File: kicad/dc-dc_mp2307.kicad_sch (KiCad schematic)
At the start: 20 parts

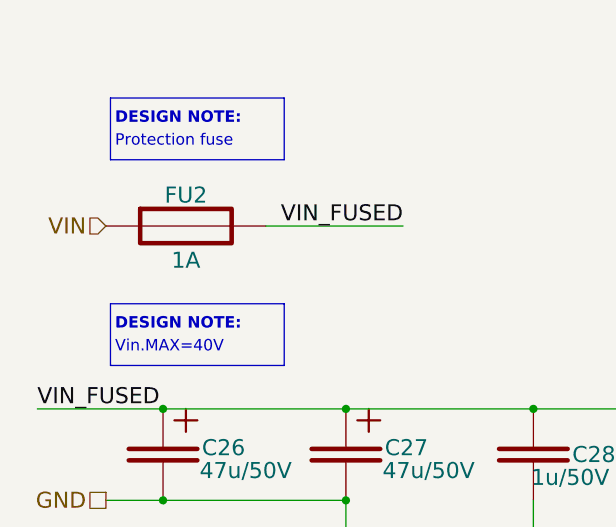
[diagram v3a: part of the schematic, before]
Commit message: Add Vin.MIN=5.5V to schematic DC-DC note
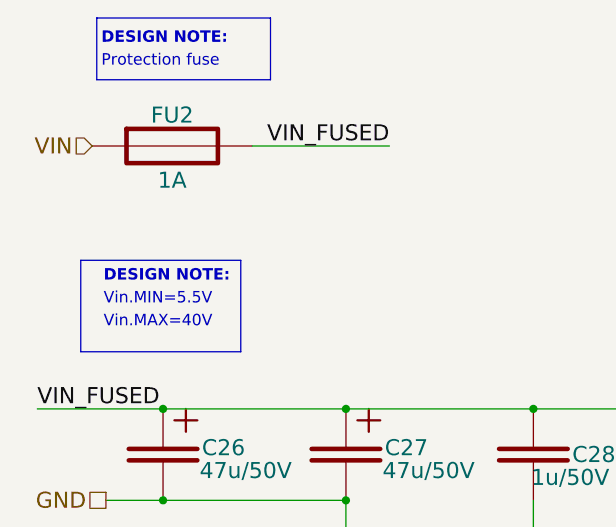
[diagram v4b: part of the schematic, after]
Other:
- note added: "Vin.MIN=5.5V"
- moved on the sheet: FU2
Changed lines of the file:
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@@
   (junction (at 78.232 69.85) (diameter 0) (color 0 0 0 0)
   )
-  (polyline (pts (xy 50.546 42.164) (xy 31.242 42.164))
+  (polyline (pts (xy 49.022 33.274) (xy 29.718 33.274))
     (stroke (width 0) (type default) (color 0 132 132 1))
   )
@@
     (stroke (width 0) (type default) (color 0 0 0 0))
   )
-  (polyline (pts (xy 31.242 58.166) (xy 31.242 65.024))
+  (polyline (pts (xy 27.94 53.34) (xy 27.94 63.5))
     (stroke (width 0) (type default) (color 0 132 132 1))
   )
@@
     (stroke (width 0) (type default) (color 0 0 0 0))
   )
-  (polyline (pts (xy 50.546 65.024) (xy 31.242 65.024))
+  (polyline (pts (xy 45.72 63.5) (xy 27.94 63.5))
     (stroke (width 0) (type default) (color 0 132 132 1))
   )
@@
     (stroke (width 0) (type default) (color 0 0 0 0))
   )
-  (polyline (pts (xy 50.546 35.306) (xy 50.546 42.164))
+  (polyline (pts (xy 49.022 26.416) (xy 49.022 33.274))
     (stroke (width 0) (type default) (color 0 132 132 1))
   )
@@
     (stroke (width 0) (type default) (color 0 0 0 0))
   )
-  (polyline (pts (xy 31.242 35.306) (xy 31.242 42.164))
+  (polyline (pts (xy 29.718 26.416) (xy 29.718 33.274))
     (stroke (width 0) (type default) (color 0 132 132 1))
   )
@@
     (stroke (width 0) (type default) (color 0 0 0 0))
   )
-  (polyline (pts (xy 50.546 58.166) (xy 50.546 65.024))
+  (polyline (pts (xy 45.72 53.34) (xy 45.72 63.5))
     (stroke (width 0) (type default) (color 0 132 132 1))
   )
@@
     (stroke (width 0) (type default) (color 0 0 0 0))
   )
-  (wire (pts (xy 48.514 49.53) (xy 63.754 49.53))
+  (wire (pts (xy 46.99 40.64) (xy 62.23 40.64))
     (stroke (width 0) (type default) (color 0 0 0 0))
   )
@@
     (stroke (width 0) (type default) (color 0 0 0 0))
   )
-  (polyline (pts (xy 31.242 35.306) (xy 50.546 35.306))
+  (polyline (pts (xy 29.718 26.416) (xy 49.022 26.416))
     (stroke (width 0) (type default) (color 0 132 132 1))
   )
@@
     (stroke (width 0) (type default) (color 0 0 0 0))
   )
-  (polyline (pts (xy 31.242 58.166) (xy 50.546 58.166))
+  (polyline (pts (xy 27.94 53.34) (xy 45.72 53.34))
     (stroke (width 0) (type default) (color 0 132 132 1))
   )
   (wire (pts (xy 57.404 80.01) (xy 57.404 118.11))
     (stroke (width 0) (type default) (color 0 0 0 0))
+  )
+  (text "Vin.MIN=5.5V" (at 30.48 58.42 0)
+    (effects (font (size 1.27 1.27)) (justify left bottom))
   )
   (text "D=(Vout/Vin)*100%=(5V/12V)*100%=41.67%" (at 76.962 124.968 0)
@@
     (effects (font (size 1.27 1.27)) (justify left bottom))
   )
+  (text "Vin.MAX=40V" (at 30.48 60.96 0)
+    (effects (font (size 1.27 1.27)) (justify left bottom))
+  )
   (text "Vout=Vref*(R1+R2/R2)=5,043" (at 77.216 134.62 0)
     (effects (font (size 1.27 1.27)) (justify left bottom))
@@
     (effects (font (size 1.27 1.27) (thickness 0.254) bold) (justify left bottom))
   )
-  (text "Protection fuse" (at 31.75 40.894 0)
-    (effects (font (size 1.27 1.27)) (justify left bottom))
-  )
-  (text "Vin.MAX=40V" (at 31.75 63.754 0)
-    (effects (font (size 1.27 1.27)) (justify left bottom))
-  )
-  (text "DESIGN NOTE:" (at 31.75 38.354 0)
+  (text "Protection fuse" (at 30.226 32.004 0)
+    (effects (font (size 1.27 1.27)) (justify left bottom))
+  )
+  (text "DESIGN NOTE:" (at 30.226 29.464 0)
     (effects (font (size 1.27 1.27) (thickness 0.254) bold) (justify left bottom))
   )
@@
     (effects (font (size 1.27 1.27) (thickness 0.254) bold) (justify left bottom))
   )
-  (text "DESIGN NOTE:" (at 31.75 61.214 0)
+  (text "DESIGN NOTE:" (at 30.48 55.88 0)
     (effects (font (size 1.27 1.27) (thickness 0.254) bold) (justify left bottom))
   )
@@
     (effects (font (size 1.778 1.778)) (justify right bottom))
   )
-  (label "VIN_FUSED" (at 63.754 49.53 180)
+  (label "VIN_FUSED" (at 62.23 40.64 180)
     (effects (font (size 1.778 1.778)) (justify right bottom))
   )
@@
     (effects (font (size 1.778 1.778)) (justify left bottom))
   )
-  (hierarchical_label "VIN" (shape input) (at 30.734 49.53 180)
+  (hierarchical_label "VIN" (shape input) (at 29.21 40.64 180)
     (effects (font (size 1.778 1.778)) (justify right))
   )
@@
     (pin "2")
   )
-  (symbol (lib_id "Fuses:FU_FUSE") (at 39.624 49.53 0) (unit 1)
-    (in_bom yes) (on_board yes)
-    (property "Reference" "FU2" (id 0) (at 39.624 46.101 0)
-      (effects (font (size 1.778 1.778)))
-    )
-    (property "Value" "1A" (id 1) (at 39.624 53.34 0)
-      (effects (font (size 1.778 1.778)))
-    )
-    (property "Footprint" "Fuse:Fuse_1206_3216Metric" (id 2) (at 39.624 49.53 0)
-      (effects (font (size 1.778 1.778)) hide)
-    )
-    (property "Datasheet" "" (id 3) (at 39.624 49.53 0)
-      (effects (font (size 1.778 1.778)) hide)
-    )
+  (symbol (lib_id "Fuses:FU_FUSE") (at 38.1 40.64 0) (unit 1)
+    (in_bom yes) (on_board yes)
+    (property "Reference" "FU2" (id 0) (at 38.1 37.211 0)
+      (effects (font (size 1.778 1.778)))
+    )
+    (property "Value" "1A" (id 1) (at 38.1 44.45 0)
+      (effects (font (size 1.778 1.778)))
+    )
+    (property "Footprint" "Fuse:Fuse_1206_3216Metric" (id 2) (at 38.1 40.64 0)
+      (effects (font (size 1.778 1.778)) hide)
+    )
+    (property "Datasheet" "" (id 3) (at 38.1 40.64 0)
+      (effects (font (size 1.778 1.778)) hide)
+    )

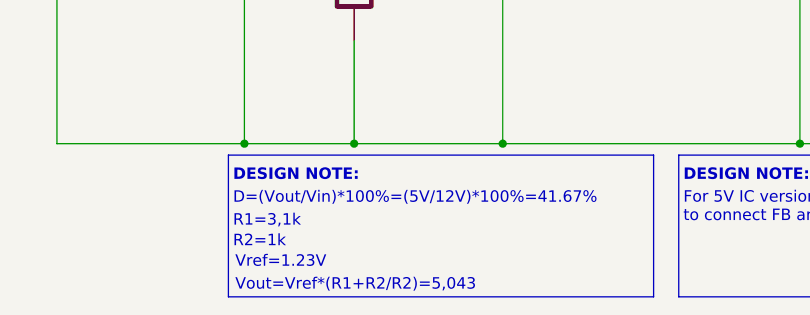
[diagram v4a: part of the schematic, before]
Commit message: Add wiring diagram; Add work ours (stage 2); refactor folders
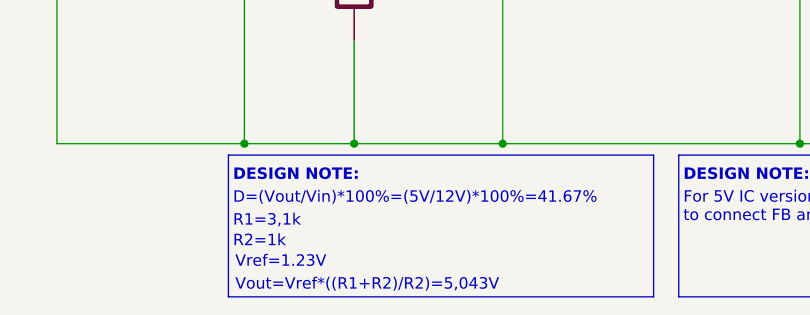
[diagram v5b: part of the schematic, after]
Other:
- note added: "Vout=Vref*((R1+R2)/R2)=5,043V"
- note removed: "Vout=Vref*(R1+R2/R2)=5,043"
- title: (none) -> RadioSens v1
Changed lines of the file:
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@@
 (kicad_sch (version 20211123) (generator eeschema)
   (paper "A4")
+  (title_block
+    (title "RadioSens v1")
+    (comment 2 "Electrical Circuit")
+  )
   (junction (at 236.22 118.11) (diameter 0) (color 0 0 0 0)
   )
@@
     (effects (font (size 1.27 1.27)) (justify left bottom))
   )
-  (text "Vout=Vref*(R1+R2/R2)=5,043" (at 77.216 134.62 0)
-    (effects (font (size 1.27 1.27)) (justify left bottom))
-  )
+  (text "Vout=Vref*((R1+R2)/R2)=5,043V" (at 77.216 134.62 0)
+    (effects (font (size 1.27 1.27)) (justify left bottom))
+  )

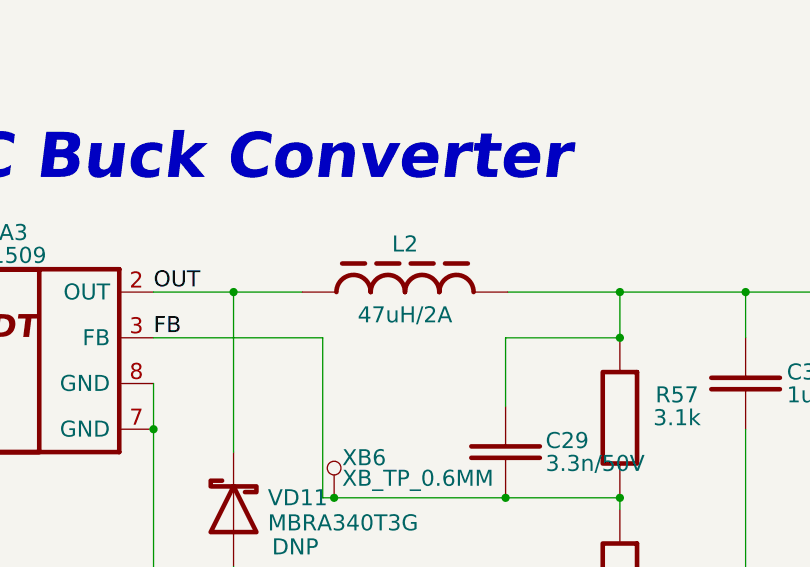
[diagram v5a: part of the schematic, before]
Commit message: update: to 7.0 ver and add fiducials
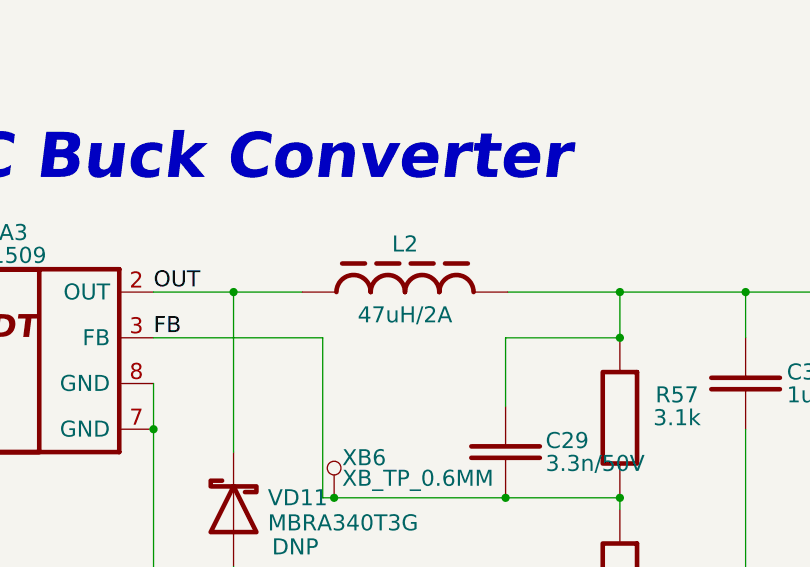
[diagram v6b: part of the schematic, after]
